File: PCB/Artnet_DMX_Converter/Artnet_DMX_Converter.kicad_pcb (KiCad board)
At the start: 4 copper layers, 100 x 72 mm, 199 parts, among them IC1 NPM1300-QEAA-R7, J1 Conn_01x03_MountingPin, J10 XLR5, J11 XLR3, J12 IDC, J13 Conn_02x04, J2 USB_C_Receptacle_USB2.0_14P, J3 RJ45, J4 XLR5, J5 XLR3, J6 XLR5, J7 XLR3, J8 XLR5, J9 XLR3, SW1 SW_Push, SW2 SW_Push, T1 FA2805, U1 RP2350B, U10 MAX3485, U11 MAX3485, U12 TXS0101DCK, U2 W25Q128JVS, U3 USBLC6-2SC6, U4 W5500, U5 VO618A-3X019T, U6 SI3402-B-GMR, U7 TLV431, U8 MAX3485, U9 MAX3485, Y1 ABM8-272-T3, Y2 ABM8-25.000MHZ-10-D1G-T

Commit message: Updated KiCad
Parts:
- moved BT1 0.50 mm to (79.0, 64.0)
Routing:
- net VDD: track 128.6 -> 123.9 mm, vias 10 -> 9
- net Net-(BT1-+): track 11.0 -> 10.5 mm
- net Net-(BT1-NTC): track 14.9 -> 14.4 mm
- net +LED: vias 17 -> 18

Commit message: Updated pcb files again....
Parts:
- moved H3 2.00 mm to (88.0, 87.0)
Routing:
- net +LED: track 287.8 -> 296.4 mm, vias 18 -> 17
- net /Ethernet/CT1: track 65.8 -> 73.2 mm
- net Net-(BT1-NTC): track 14.4 -> 18.4 mm
- net /Ethernet/SP2: track 48.1 -> 46.6 mm
- net /Ethernet/CT2: track 80.7 -> 81.6 mm
- net /Ethernet/V+: track 51.4 -> 50.5 mm, vias 6 -> 5
- net /Ethernet/SP1: track 51.5 -> 52.2 mm

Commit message: Updated PCB files
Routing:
- net GND: vias 116 -> 117
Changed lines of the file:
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@@
+	)
+	(via
+		(at 64.95 58.2)
+		(size 0.6)
+		(drill 0.3)
+		(layers "F.Cu" "B.Cu")
+		(free yes)
+		(net 11)
 	)
 	(via

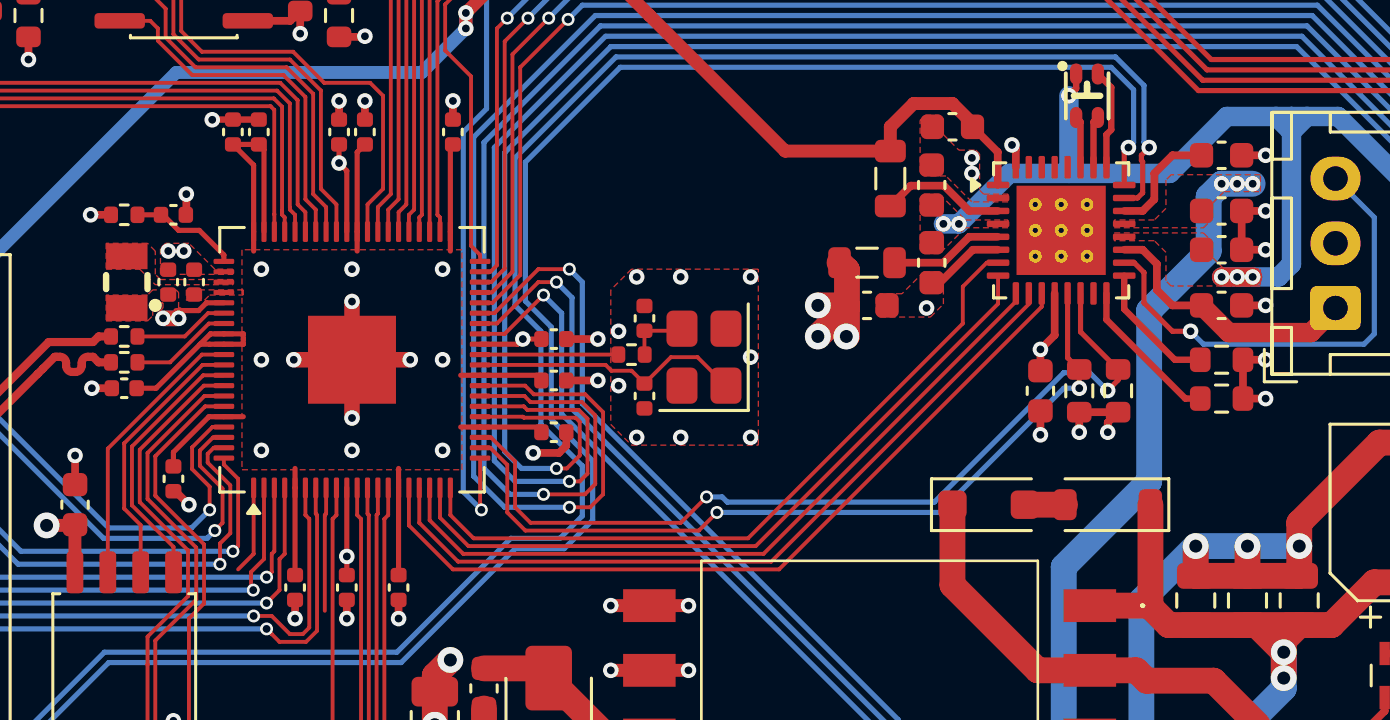
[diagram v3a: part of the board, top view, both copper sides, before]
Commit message: Added firmware and some changes to the PCB
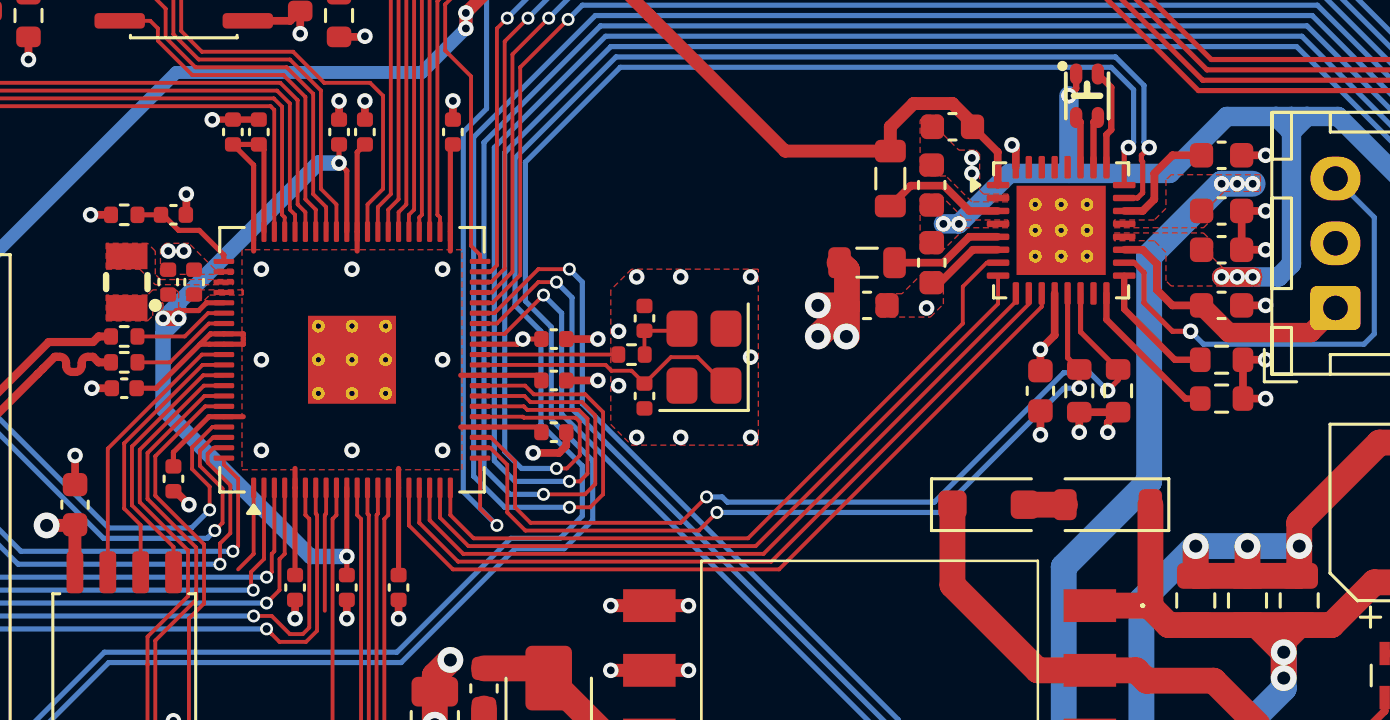
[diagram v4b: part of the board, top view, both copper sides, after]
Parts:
- added ?: , , F.Cu at (41.0, 67.3)
- added ?: , , F.Cu at (42.3, 66.0)
- added ?: , , F.Cu at (42.3, 64.7)
- added ?: , , F.Cu at (39.7, 64.7)
- added ?: , , F.Cu at (42.3, 67.3)
- added ?: , , F.Cu at (41.0, 66.0)
- added ?: , , F.Cu at (39.7, 67.3)
- added ?: , , F.Cu at (39.7, 66.0)
- added ?: , , F.Cu at (41.0, 64.7)
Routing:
- net GND: track 147.9 -> 138.9 mm, vias 117 -> 113
- net +1V1: track 45.0 -> 48.8 mm
- net /DMX/LEDs: track 56.9 -> 58.6 mm
